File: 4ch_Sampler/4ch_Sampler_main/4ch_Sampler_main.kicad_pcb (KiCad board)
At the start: 2 copper layers, 30 x 100 mm, 33 parts, among them J6 POWER, U2 NJM2372D

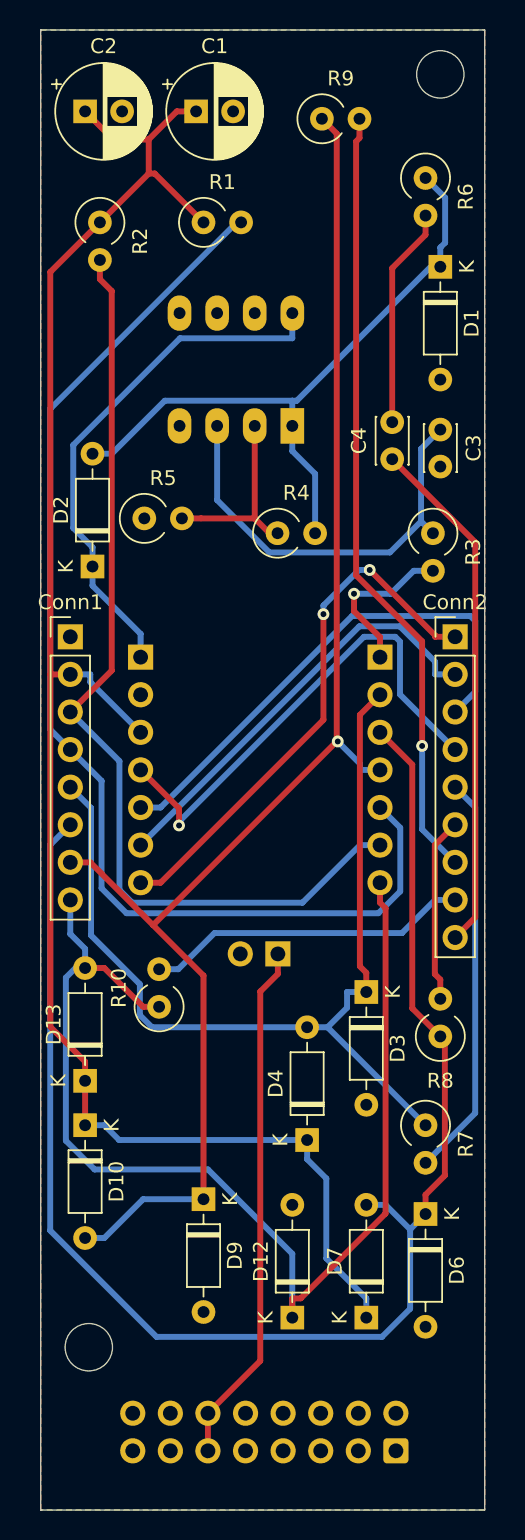
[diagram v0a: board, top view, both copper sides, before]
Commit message: Ground plane fixed
Ground plane unconnected fixed and front pcb headers fliped to the back (footprint)
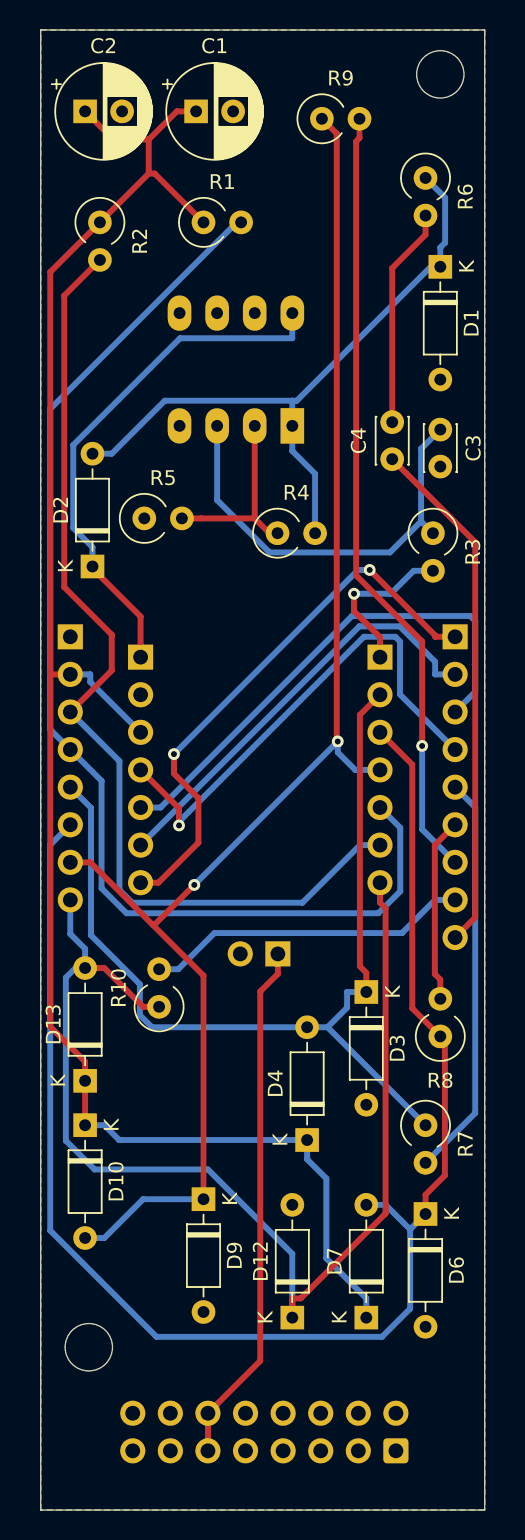
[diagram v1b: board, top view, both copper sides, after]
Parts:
- Conn1, Conn2: moved to B.Cu
- turned Conn1 to 180 degrees
- turned Conn2 to 180 degrees
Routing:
- net Net-(Brd1-Pad3): track 65.0 -> 67.0 mm
- net TOUCH_SENSOR1: track 36.5 -> 37.8 mm
- net Net-(D10-Pad2): track 100.4 -> 100.6 mm, vias 1 -> 2

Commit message: orientation headers and capacitors
Did a update on the headers. In 3d view some headers where pins changed to sockets. Did update previously on wrong board (flip header to wrong side) should be good now. Move bigger capacitors to the back of the board for more height possiblities.

Removed Gerber.zip added new gebers for this version in folders unzipped
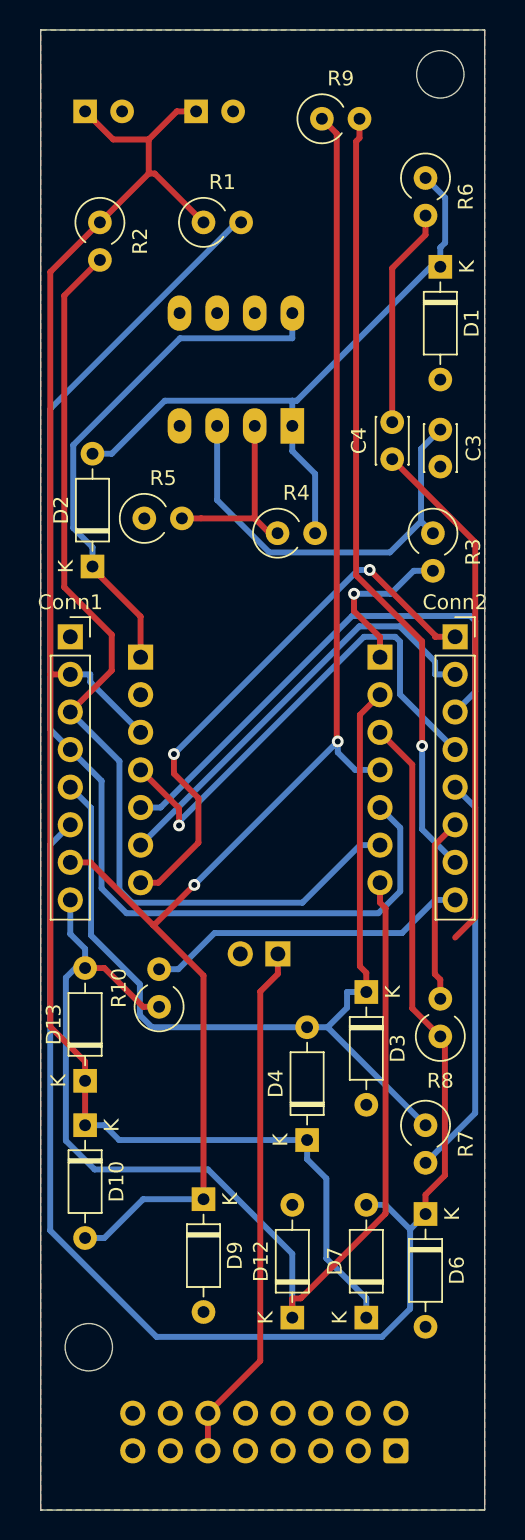
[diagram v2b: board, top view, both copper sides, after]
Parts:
- C1, C2: moved to B.Cu
- Conn1: value PinHeader_1x08_P2.54mm_Vertical -> PinSocket_1x08_P2.54mm_Vertical; footprint Connector_PinHeader_2.54mm:PinHeader_1x08_P2.54mm_Vertical -> Connector_PinSocket_2.54mm:PinSocket_1x08_P2.54mm_Vertical; moved to F.Cu
- Conn2: value PinHeader_1x09_P2.54mm_Vertical -> PinSocket_1x08_P2.54mm_Vertical; footprint Connector_PinHeader_2.54mm:PinHeader_1x09_P2.54mm_Vertical -> Connector_PinSocket_2.54mm:PinSocket_1x08_P2.54mm_Vertical; moved to F.Cu
- Xiao1, Xiao2: footprint Connector_PinHeader_2.54mm:PinHeader_1x07_P2.54mm_Vertical -> Connector_PinSocket_2.54mm:PinSocket_1x07_P2.54mm_Vertical
- turned Conn1 to 0 degrees
- turned Conn2 to 0 degrees
